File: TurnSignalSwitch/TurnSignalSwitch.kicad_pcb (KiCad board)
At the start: 2 copper layers, 88.4 x 25.4 mm, 0 parts

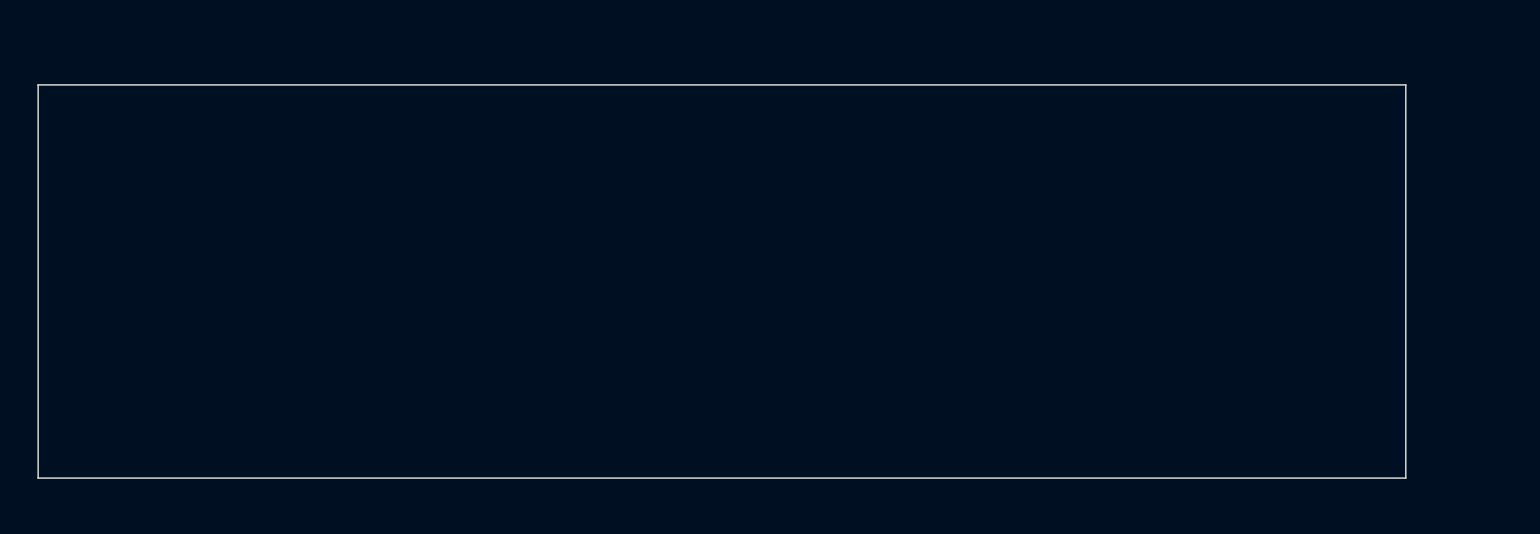
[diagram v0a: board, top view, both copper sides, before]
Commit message: Completed control boards.
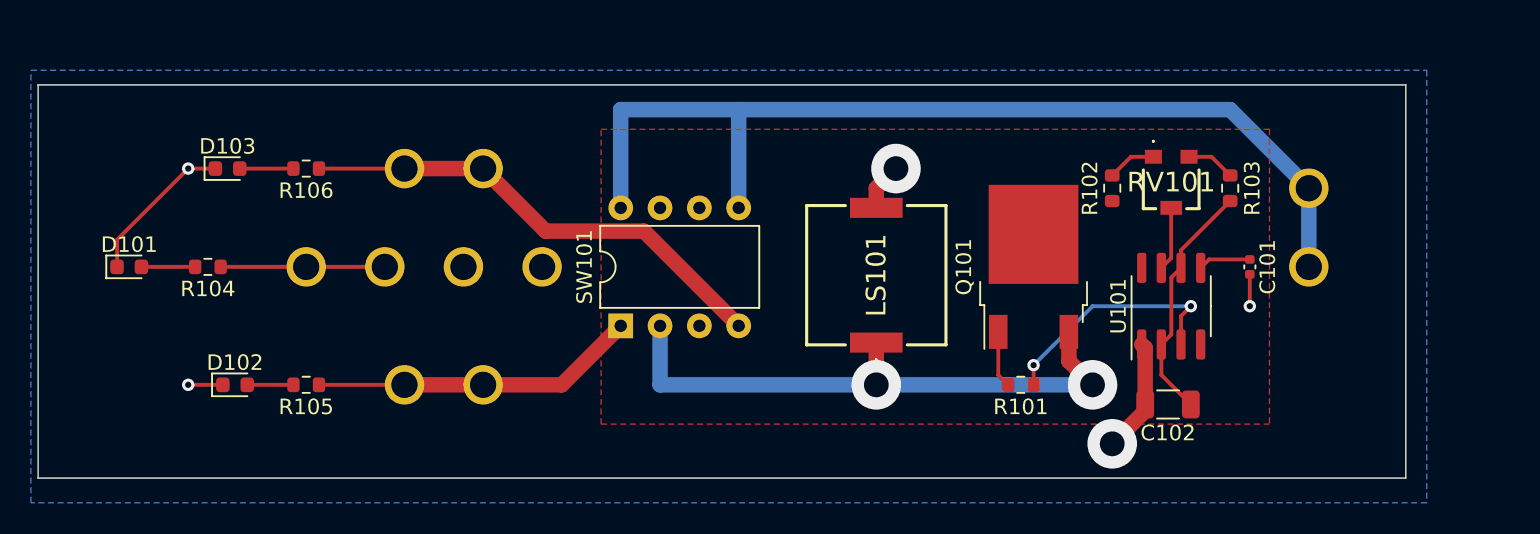
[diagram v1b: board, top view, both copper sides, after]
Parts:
- added C101: .01uf, Capacitor_SMD:C_0402_1005Metric, F.Cu at (165.1, 68.6)
- added C102: 10uf, Capacitor_SMD:C_1206_3216Metric, F.Cu at (159.8, 77.5)
- added D101: Brake, LED_SMD:LED_0603_1608Metric, F.Cu at (92.7, 68.6)
- added D102: Left, LED_SMD:LED_0603_1608Metric, F.Cu at (99.5, 76.2)
- added D103: Right, LED_SMD:LED_0603_1608Metric, F.Cu at (99.1, 62.2)
- added J0: C-, SpadeLugs:197054303, B.Cu at (114.3, 68.6)
- added J101: Brake+, SpadeLugs:197054303, B.Cu at (109.2, 68.6)
- added J102: Battery+, SpadeLugs:197054303, B.Cu at (168.9, 68.6)
- added J103: Left+, SpadeLugs:197054303, B.Cu at (115.6, 76.2)
- added J104: Right+, SpadeLugs:197054303, B.Cu at (115.6, 62.2)
- added LS101: PKMCS0909E4000-R1, Piezo:PKMCS0909E4000R1, F.Cu at (141.0, 69.1)
- added Q101: MJD112, Package_TO_SOT_SMD:TO-252-2, F.Cu at (151.1, 68.6)
- added R101: 1K, Resistor_SMD:R_0603_1608Metric, F.Cu at (150.3, 76.2)
- added R102: 1K, Resistor_SMD:R_0603_1608Metric, F.Cu at (156.2, 63.5)
- added R103: 1K, Resistor_SMD:R_0603_1608Metric, F.Cu at (163.8, 63.5)
- added R104: 1K, Resistor_SMD:R_0603_1608Metric, F.Cu at (97.8, 68.6)
- added R105: 1K, Resistor_SMD:R_0603_1608Metric, F.Cu at (104.1, 76.2)
- added R106: 1K, Resistor_SMD:R_0603_1608Metric, F.Cu at (104.1, 62.2)
- added RV101: 100K, BournsPVG3A:PVG3A103C01R00, F.Cu at (160.0, 63.1)
- added SW101: SW_Rotary2x3, Package_DIP:DIP-8_W7.62mm, F.Cu at (124.5, 72.4)
- added U101: LM555xM, Package_SO:SOIC-8_3.9x4.9mm_P1.27mm, F.Cu at (160.0, 71.1)
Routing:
- net +12V: track 0.00 -> 64.3 mm
- net /TSBlink: track 0.00 -> 38.5 mm, vias 0 -> 2
- net Net-(J104-Pad1): track 0.00 -> 31.3 mm
- net GNDPWR: track 0.00 -> 24.8 mm, vias 0 -> 5
- net Net-(J103-Pad1): track 0.00 -> 21.1 mm
- net Net-(C102-Pad1): track 0.00 -> 15.8 mm
- net /TSq: track 0.00 -> 15.7 mm, vias 0 -> 2
- net Net-(J101-Pad1): track 0.00 -> 10.6 mm
- net Net-(RV101-Pad2): track 0.00 -> 4.14 mm
- net Net-(Q101-Pad1): track 0.00 -> 3.68 mm
- net Net-(D103-Pad2): track 0.00 -> 3.47 mm
- net Net-(D101-Pad2): track 0.00 -> 3.47 mm
- net Net-(C101-Pad1): track 0.00 -> 3.40 mm
- net Net-(R103-Pad1): track 0.00 -> 3.16 mm
- net Net-(R102-Pad2): track 0.00 -> 3.16 mm
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- added copper zone on F.Cu, net /TSPow
- added copper zone on B.Cu, net GNDPWR

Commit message: Mounting holes and dims.
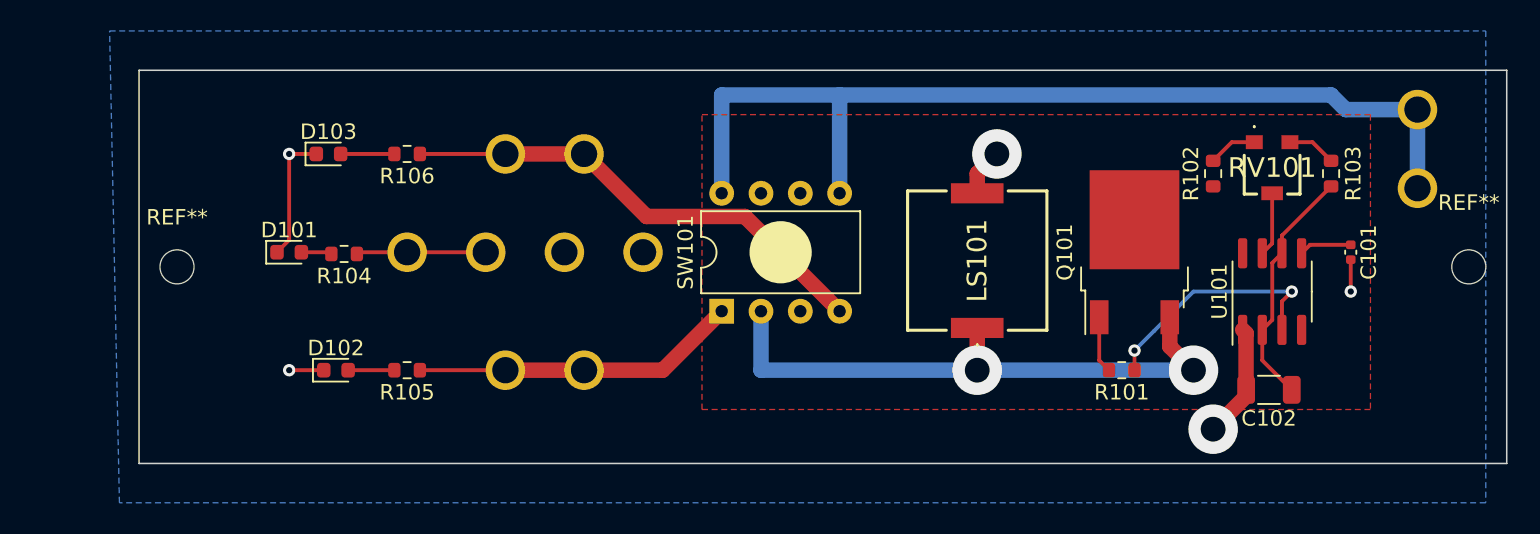
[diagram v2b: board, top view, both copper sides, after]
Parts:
- added REF**: MountingHole_2.2mm_M2, MountingHole:MountingHole_2.2mm_M2, F.Cu at (95.8, 68.6)
- added REF**: MountingHole_2.2mm_M2, MountingHole:MountingHole_2.2mm_M2, F.Cu at (179.2, 68.6)
- moved J102 12.3 mm to (175.9, 58.4), turned to -90 degrees
- moved D101 10.4 mm to (103.0, 67.6)
- moved R104 8.84 mm to (106.6, 67.7)
- moved J103 6.59 mm to (122.1, 75.3)
- moved LS101 6.59 mm to (147.5, 68.2)
- moved C101 6.59 mm to (171.6, 67.6)
- moved C102 6.59 mm to (166.3, 76.5)
- moved J104 6.59 mm to (122.1, 61.3)
- moved Q101 6.59 mm to (157.7, 67.6)
- moved D102 6.59 mm to (106.1, 75.3)
- moved D103 6.59 mm to (105.6, 61.3)
- moved R105 6.59 mm to (110.7, 75.3)
- moved R106 6.59 mm to (110.7, 61.3)
- moved SW101 6.59 mm to (131.0, 71.4)
- moved J0 6.59 mm to (120.8, 67.6)
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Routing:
- net Net-(J101-Pad1): track 10.6 -> 8.37 mm
- net GNDPWR: track 24.8 -> 23.2 mm
- net Net-(D101-Pad2): track 3.47 -> 1.98 mm
- net +12V: track 64.3 -> 63.1 mm
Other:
- board size 88.4 x 25.4 mm -> 88.3 x 25.4 mm
